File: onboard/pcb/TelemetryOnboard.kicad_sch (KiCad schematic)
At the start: 140 parts, among them J1 USB-C, J2 USB-C, J3 RFPC-SMA28-F, J4 RFPC-SMA28-F, J5 Molex_MicroFit_2pin, M1 M4 Mounting Hole, M2 M4 Mounting Hole, M3 M4 Mounting Hole, M4 M4 Mounting Hole, Q1 MMBT4401-TP, U1 CP2102N, U2 CP2102N, U3 AVR128DB64x-xPT, U4 RC1780HP-RC232, U5 RC1701HP-RC232, U6 W25Q80DVSSIG

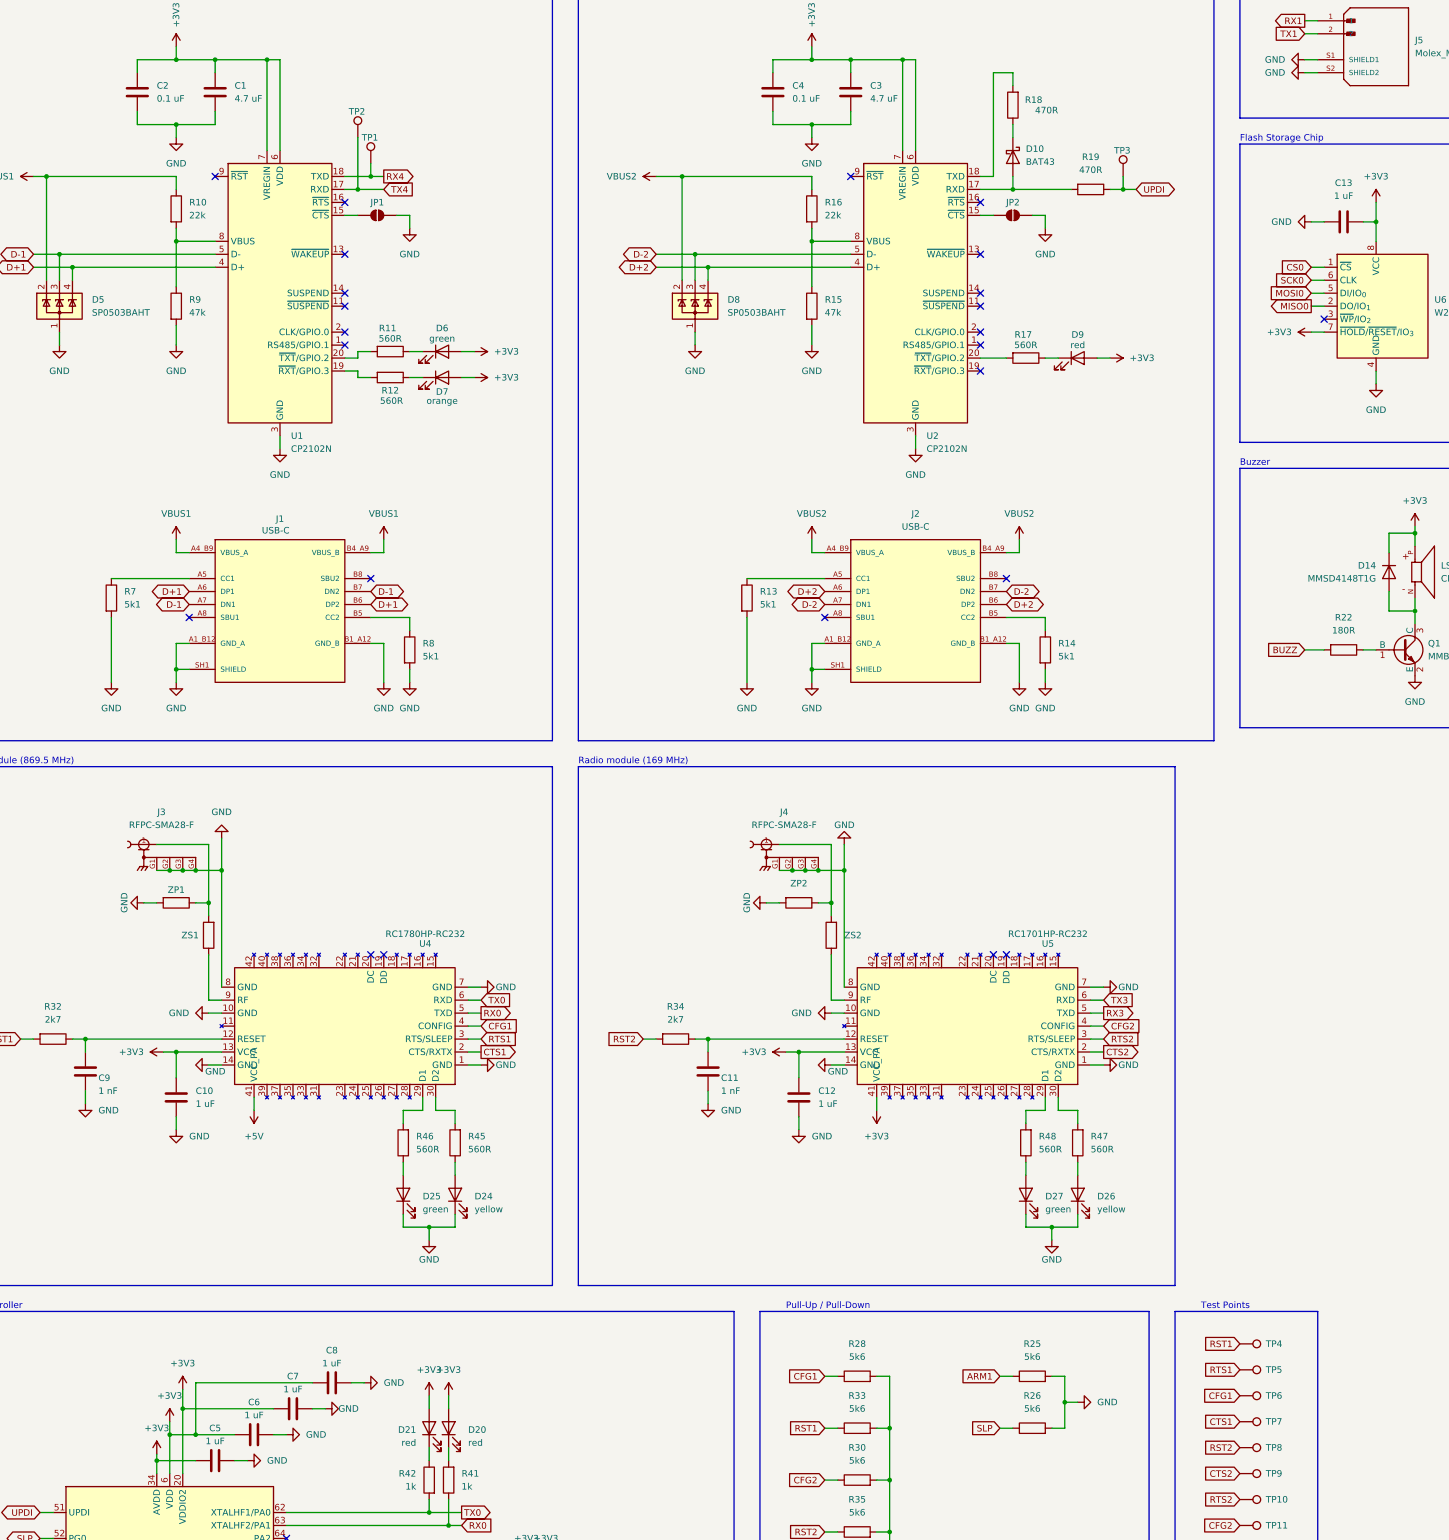
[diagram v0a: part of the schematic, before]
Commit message: add purchase links to components
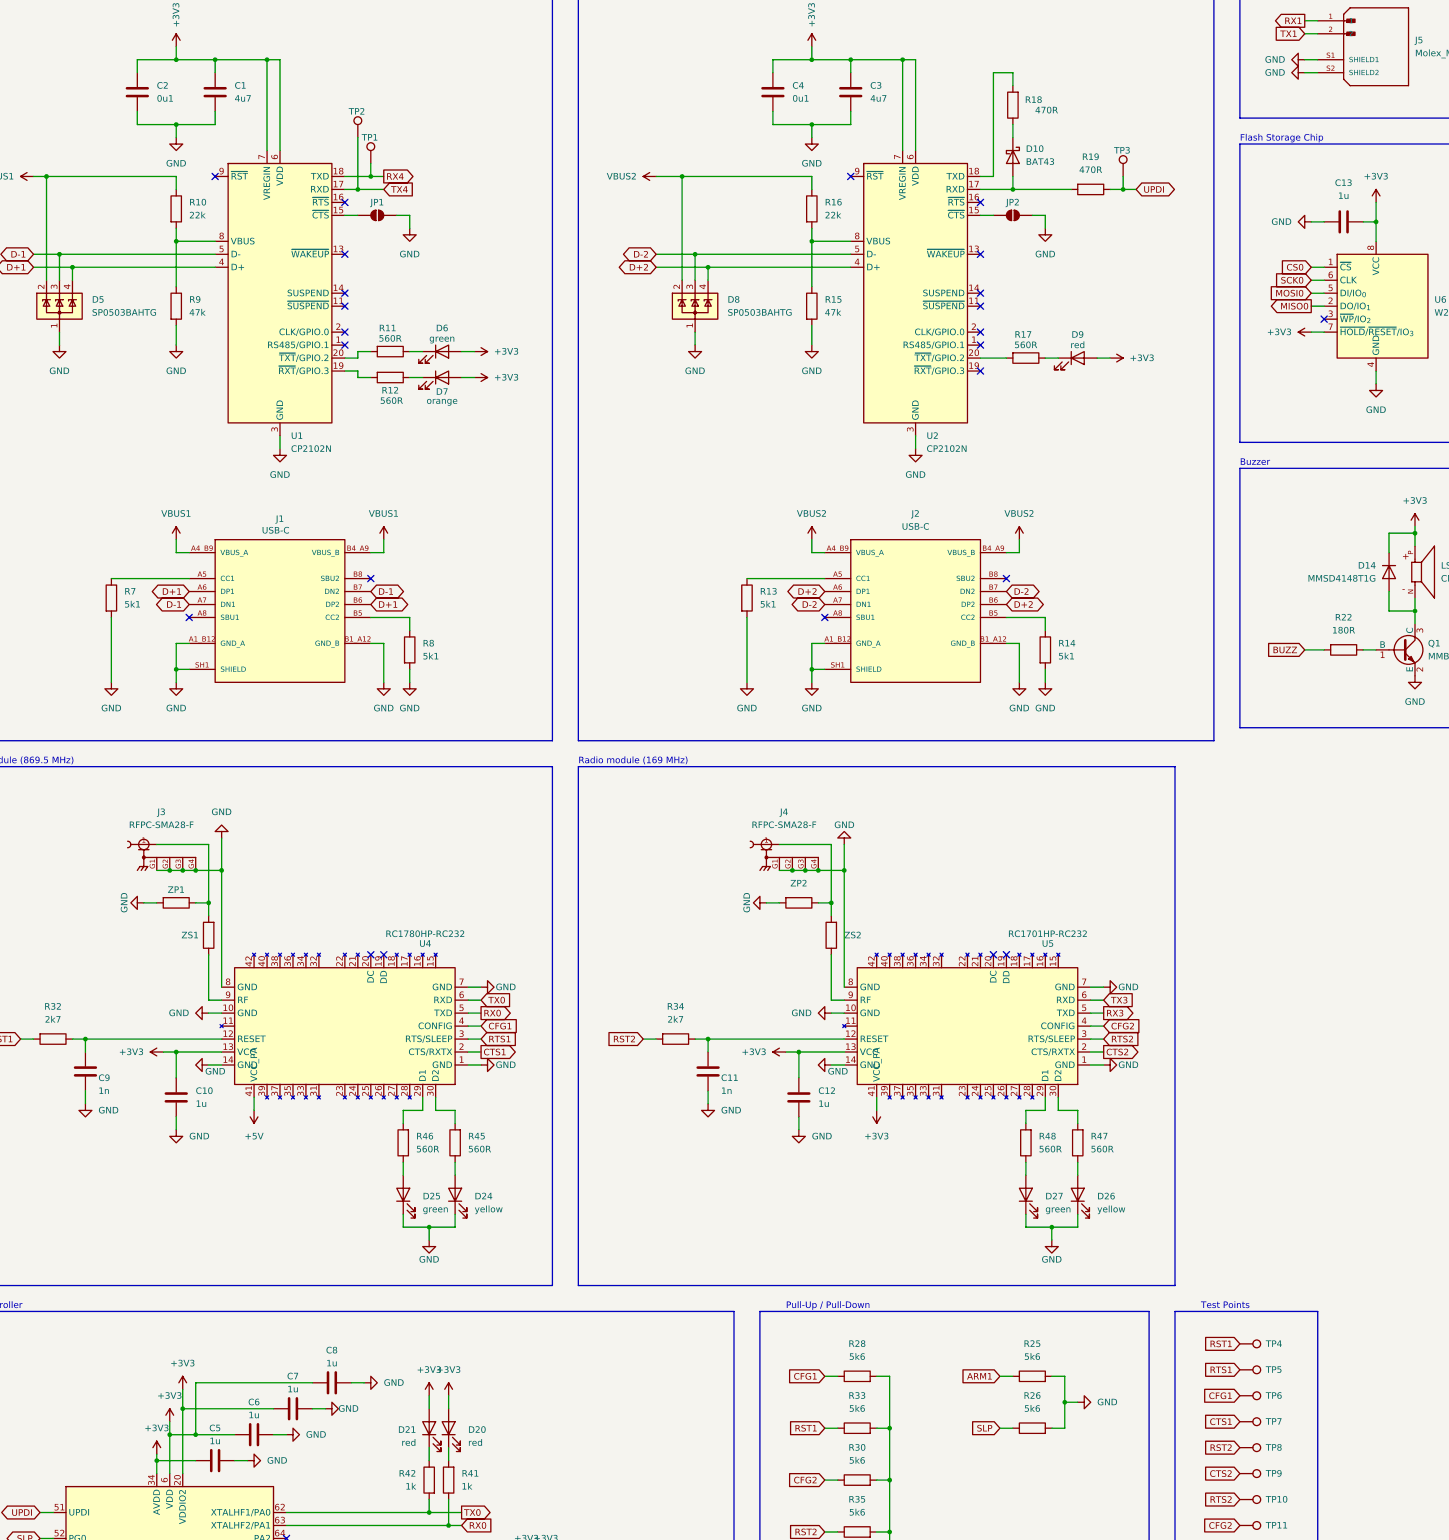
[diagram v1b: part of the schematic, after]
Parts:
- C1, C3: value 4.7 uF -> 4u7; Purchase-URL (none) -> https://www.digikey.de/de/products/detail/samsung-electro-m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
- C10, C12, C13, C5, C6, C7, C8: value 1 uF -> 1u; Purchase-URL (none) -> https://www.digikey.de/de/products/detail/samsung-electro-m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
- C11, C9: value 1 nF -> 1n; Purchase-URL (none) -> https://www.digikey.de/de/products/detail/samsung-electro-m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
- C2, C4: value 0.1 uF -> 0u1; Purchase-URL (none) -> https://www.digikey.de/de/products/detail/samsung-electro-m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
- D1, D15, D16, D17, D18, D19, D2, D24, D26, D3, D7: Purchase-URL (none) -> https://www.digikey.de/de/products/detail/liteon/LTST-C170K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
- D10, Q1: Purchase-URL (none) -> https://www.digikey.de/de/products/detail/mcc-micro-commerc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
- D11, D12, D20, D21, D22, D23, D25, D27, D28, D29, D6, D9: Purchase-URL (none) -> https://www.digikey.de/de/products/detail/liteon/LTST-C171K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
- D13: Purchase-URL (none) -> https://www.digikey.de/de/products/detail/w%C3%BCrth-elektr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
- D14: Purchase-URL (none) -> https://www.digikey.de/de/products/detail/onsemi/MMSD4148T1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
- D4: Purchase-URL (none) -> https://www.digikey.de/de/products/detail/cree-led/CLP6C-FK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
- D5, D8: value SP0503BAHT -> SP0503BAHTG; Purchase-URL (none) -> https://www.digikey.de/de/products/detail/littelfuse-inc/SP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
- J1, J2: Purchase-URL (none) -> https://www.digikey.de/de/products/detail/gct/USB4216-03-A/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
- J3, J4: Purchase-URL (none) -> https://www.digikey.de/de/products/detail/gct/RFPC-SMA28-F/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
- J5: Purchase-URL (none) -> https://www.digikey.de/de/products/detail/molex/0436500203/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
- JL1, JL2, JR1, JR2: Purchase-URL (none) -> https://www.digikey.de/de/products/detail/samtec-inc/ESQ-10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
- LS1: Purchase-URL (none) -> https://www.digikey.de/de/products/detail/same-sky-formerly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
- R1, R10, R11, R12, R13, R14, R15, R16, R17, R18, R19, R2, R20, R21, R22, R23, R24, R25, R26, R27, R28, R29, R3, R30, R31, R32, R33, R34, R35, R36, R37, R38, R39, R4, R40, R41, R42, R43, R44, R45, R46, R47, R48, R49, R5, R50, R6, R7, R8, R9: Purchase-URL (none) -> https://www.digikey.de/de/products/detail/stackpole-electro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
- U1, U2: Purchase-URL (none) -> https://www.digikey.de/de/products/detail/silicon-labs/CP21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
- U5: Purchase-URL (none) -> https://www.digikey.de/de/products/detail/radiocrafts-as/RC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
- U6: Purchase-URL (none) -> https://www.digikey.de/de/products/detail/winbond-electroni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

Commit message: add label to radio module leds
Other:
- note added: "RX"
- note added: "TX"
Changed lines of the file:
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@@
 		)
 	)
+	(text "RX"
+		(exclude_from_sim no)
+		(at 117.602 374.904 0)
+		(effects
+			(font
+				(size 1.27 1.27)
+			)
+		)
+	)
+	(text "TX"
+		(exclude_from_sim no)
+		(at 225.552 374.904 0)
+		(effects
+			(font
+				(size 1.27 1.27)
+			)
+		)
+	)
 	(text "USB UART"
 		(exclude_from_sim no)
@@
 		)
 	)
+	(text "RX"
+		(exclude_from_sim no)
+		(at 239.776 374.904 0)
+		(effects
+			(font
+				(size 1.27 1.27)
+			)
+		)
+	)
 	(text "Debug LEDs"
 		(exclude_from_sim no)
@@
 		)
 	)
+	(text "TX"
+		(exclude_from_sim no)
+		(at 103.632 374.904 0)
+		(effects
+			(font
+				(size 1.27 1.27)
+			)
+		)
+	)
 	(text "ESD Protection"
 		(exclude_from_sim no)
@@
 		)
 	)
-	(global_label "GND"
-		(shape bidirectional)
-		(at 102.87 43.18 0)
-		(fields_autoplaced yes)
-		(effects
-			(font
-				(size 1.27 1.27)
-			)
-			(justify left)
-		)
-		(property "Intersheetrefs" "${INTERSHEET_REFS}"
-			(at 110.837 43.18 0)
-			(effects
-				(font
-					(size 1.27 1.27)
-				)
-				(justify left)
-				(hide yes)
-			)
-		)
-	)
 	(global_label "LED 2"
 		(shape output)
@@
 					(unit 1)
 				)
+			)
+		)
+	)
+	(symbol
+		(lib_id "power:GND")
+		(at 102.87 43.18 90)
+		(unit 1)
+		(exclude_from_sim no)
+		(in_bom yes)
+		(on_board yes)
+		(dnp no)
+		(fields_autoplaced yes)
+		(property "Reference" "#PWR096"
+			(at 109.22 43.18 0)
+			(effects
+				(font
+					(size 1.27 1.27)
+				)
+				(hide yes)
+			)
+		)
+		(property "Value" "GND"
+			(at 106.68 43.1799 90)
+			(effects
+				(font
+					(size 1.27 1.27)
+				)
+				(justify right)
+			)
+		)
+		(property "Footprint" ""
+			(at 102.87 43.18 0)
+			(effects
+				(font
+					(size 1.27 1.27)
+				)
+				(hide yes)
+			)
+		)
+		(property "Datasheet" ""
+			(at 102.87 43.18 0)
+			(effects
+				(font
+					(size 1.27 1.27)
+				)
+				(hide yes)
+			)
+		)
+		(property "Description" "Power symbol creates a global label with name \"GND\" , ground"
+			(at 102.87 43.18 0)
+			(effects
+				(font
+					(size 1.27 1.27)
+				)
+				(hide yes)
+			)
+		)
+		(pin "1"
+		)
+		(instances
+			(project "TelemetryOnboard"
+				(path "/a51e9d97-2dc7-47e6-bab2-df98d7ad5ab9"
+					(reference "#PWR096")
+					(unit 1)
+				)

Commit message: add drawing sheet informations
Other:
- company: (none) -> Spaceflight Rocketry Giessen e.V.
- title: (none) -> Telemetry Onboard PCB
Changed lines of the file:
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@@
 	(generator_version "9.0")
 	(paper "A2" portrait)
+	(title_block
+		(title "Telemetry Onboard PCB")
+		(date "2026-03-01")
+		(company "Spaceflight Rocketry Giessen e.V.")
+	)
 	(rectangle
 		(start 17.78 284.48)
